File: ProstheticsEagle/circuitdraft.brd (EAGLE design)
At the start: 63 x 37 mm, 49 parts, among them IC1 BQ25887RGER, IC2 TPS54627DDAR, Q1 16 MHz

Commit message: ffff
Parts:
- L2: device rcl:0204/7 -> SamacSys_Parts:INDC2016X100N
- moved R9 2.48 mm to (41.7, 3.70)
- moved C18 1.00 mm to (42.2, 8.78)
- renumbered SERVO1 to S1, SERVO2 to S2, SERVO3 to S3, SERVO4 to S4, SERVO5 to S5

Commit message: fff
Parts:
- moved C18 0.40 mm to (41.9, 8.91)
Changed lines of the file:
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@@
 <attribute name="SPICEPREFIX" value="C" x="21.51" y="19.95" size="1.778" layer="27" rot="R90" display="off"/>
 </element>
-<element name="C18" library="rcl" library_urn="urn:adsk.eagle:library:334" package="C0805" package3d_urn="urn:adsk.eagle:package:23617/2" value="10 uF" x="42.25" y="8.78" smashed="yes">
-<attribute name="POPULARITY" value="63" x="90.51" y="-22.97" size="1.778" layer="27" display="off"/>
-<attribute name="SPICEPREFIX" value="C" x="42.25" y="8.78" size="1.778" layer="27" display="off"/>
+<element name="C18" library="rcl" library_urn="urn:adsk.eagle:library:334" package="C0805" package3d_urn="urn:adsk.eagle:package:23617/2" value="10 uF" x="41.869" y="8.907" smashed="yes">
+<attribute name="POPULARITY" value="63" x="90.129" y="-22.843" size="1.778" layer="27" display="off"/>
+<attribute name="SPICEPREFIX" value="C" x="41.869" y="8.907" size="1.778" layer="27" display="off"/>
 </element>
 <element name="C2" library="rcl" library_urn="urn:adsk.eagle:library:334" package="C0805" package3d_urn="urn:adsk.eagle:package:23617/2" value="22pF" x="25.5" y="6.66" smashed="yes" rot="R180">
@@
 </element>
 <element name="S3" library="pinhead" library_urn="urn:adsk.eagle:library:325" package="1X03" package3d_urn="urn:adsk.eagle:package:22458/2" value="" x="44.27" y="12.13" smashed="yes">
-<attribute name="NAME" x="40.6838" y="8.3788" size="1.27" layer="25" font="vector" ratio="10"/>
+<attribute name="NAME" x="49.1928" y="11.8078" size="1.27" layer="25" font="vector" ratio="10"/>
 <attribute name="POPULARITY" value="92" x="70.94" y="-39.94" size="1.778" layer="27" display="off"/>
 <attribute name="VALUE" x="40.46" y="8.955" size="1.27" layer="27"/>
@@
 <contactref element="L2" pad="1"/>
 <contactref element="C18" pad="1"/>
-<wire x1="37.08" y1="6.78" x2="41.3" y2="8.78" width="0" layer="19" extent="1-1"/>
+<wire x1="37.08" y1="6.78" x2="40.919" y2="8.907" width="0" layer="19" extent="1-1"/>
 <wire x1="35.14" y1="11.56" x2="37.08" y2="6.78" width="0" layer="19" extent="1-1"/>
 </signal>

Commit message: aa
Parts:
- C11, C12: value 22 pF -> 22 uF
- C4, C5: value 10 pF -> 10 uF
- C6: value .1 pF -> .1 uF
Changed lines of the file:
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@@
 <attribute name="SPICEPREFIX" value="C" x="70.33" y="19.02" size="1.778" layer="27" rot="R90" display="off"/>
 </element>
-<element name="C11" library="rcl" library_urn="urn:adsk.eagle:library:334" package="C0805" package3d_urn="urn:adsk.eagle:package:23617/2" value="22 pF" x="46.49" y="7.48" smashed="yes">
+<element name="C11" library="rcl" library_urn="urn:adsk.eagle:library:334" package="C0805" package3d_urn="urn:adsk.eagle:package:23617/2" value="22 uF" x="46.49" y="7.48" smashed="yes">
 <attribute name="NAME" x="48.539" y="7.258" size="1.27" layer="25" font="vector" ratio="10"/>
 <attribute name="POPULARITY" value="63" x="69.35" y="-24.27" size="1.778" layer="27" display="off"/>
 <attribute name="SPICEPREFIX" value="C" x="46.49" y="7.48" size="1.778" layer="27" display="off"/>
 </element>
-<element name="C12" library="rcl" library_urn="urn:adsk.eagle:library:334" package="C0805" package3d_urn="urn:adsk.eagle:package:23617/2" value="22 pF" x="46.86" y="4.97" smashed="yes">
+<element name="C12" library="rcl" library_urn="urn:adsk.eagle:library:334" package="C0805" package3d_urn="urn:adsk.eagle:package:23617/2" value="22 uF" x="46.86" y="4.97" smashed="yes">
 <attribute name="NAME" x="49.009" y="4.348" size="1.27" layer="25" font="vector" ratio="10"/>
 <attribute name="POPULARITY" value="63" x="76.07" y="-26.78" size="1.778" layer="27" display="off"/>
@@
 <attribute name="SPICEPREFIX" value="C" x="18" y="6.29" size="1.778" layer="27" display="off"/>
 </element>
-<element name="C4" library="rcl" library_urn="urn:adsk.eagle:library:334" package="C0805" package3d_urn="urn:adsk.eagle:package:23617/2" value="10 pF" x="67.98" y="27.23" smashed="yes" rot="R180">
+<element name="C4" library="rcl" library_urn="urn:adsk.eagle:library:334" package="C0805" package3d_urn="urn:adsk.eagle:package:23617/2" value="10 uF" x="67.98" y="27.23" smashed="yes" rot="R180">
 <attribute name="NAME" x="65.731" y="27.752" size="1.27" layer="25" font="vector" ratio="10" rot="R180"/>
 <attribute name="POPULARITY" value="63" x="12.1" y="51.36" size="1.778" layer="27" rot="R180" display="off"/>
 <attribute name="SPICEPREFIX" value="C" x="67.98" y="27.23" size="1.778" layer="27" rot="R180" display="off"/>
 </element>
-<element name="C5" library="rcl" library_urn="urn:adsk.eagle:library:334" package="C0805" package3d_urn="urn:adsk.eagle:package:23617/2" value="10 pF" x="29.84" y="7.54" smashed="yes">
+<element name="C5" library="rcl" library_urn="urn:adsk.eagle:library:334" package="C0805" package3d_urn="urn:adsk.eagle:package:23617/2" value="10 uF" x="29.84" y="7.54" smashed="yes">
 <attribute name="NAME" x="32.169" y="6.678" size="1.27" layer="25" font="vector" ratio="10"/>
 <attribute name="POPULARITY" value="63" x="92.07" y="-16.59" size="1.778" layer="27" display="off"/>
 <attribute name="SPICEPREFIX" value="C" x="29.84" y="7.54" size="1.778" layer="27" display="off"/>
 </element>
-<element name="C6" library="rcl" library_urn="urn:adsk.eagle:library:334" package="C0805" package3d_urn="urn:adsk.eagle:package:23617/2" value=".1 pF" x="28.39" y="3.09" smashed="yes" rot="R90">
+<element name="C6" library="rcl" library_urn="urn:adsk.eagle:library:334" package="C0805" package3d_urn="urn:adsk.eagle:package:23617/2" value=".1 uF" x="28.39" y="3.09" smashed="yes" rot="R90">
 <attribute name="NAME" x="28.912" y="5.139" size="1.27" layer="25" font="vector" ratio="10" rot="R90"/>
 <attribute name="POPULARITY" value="63" x="60.14" y="57.7" size="1.778" layer="27" rot="R90" display="off"/>

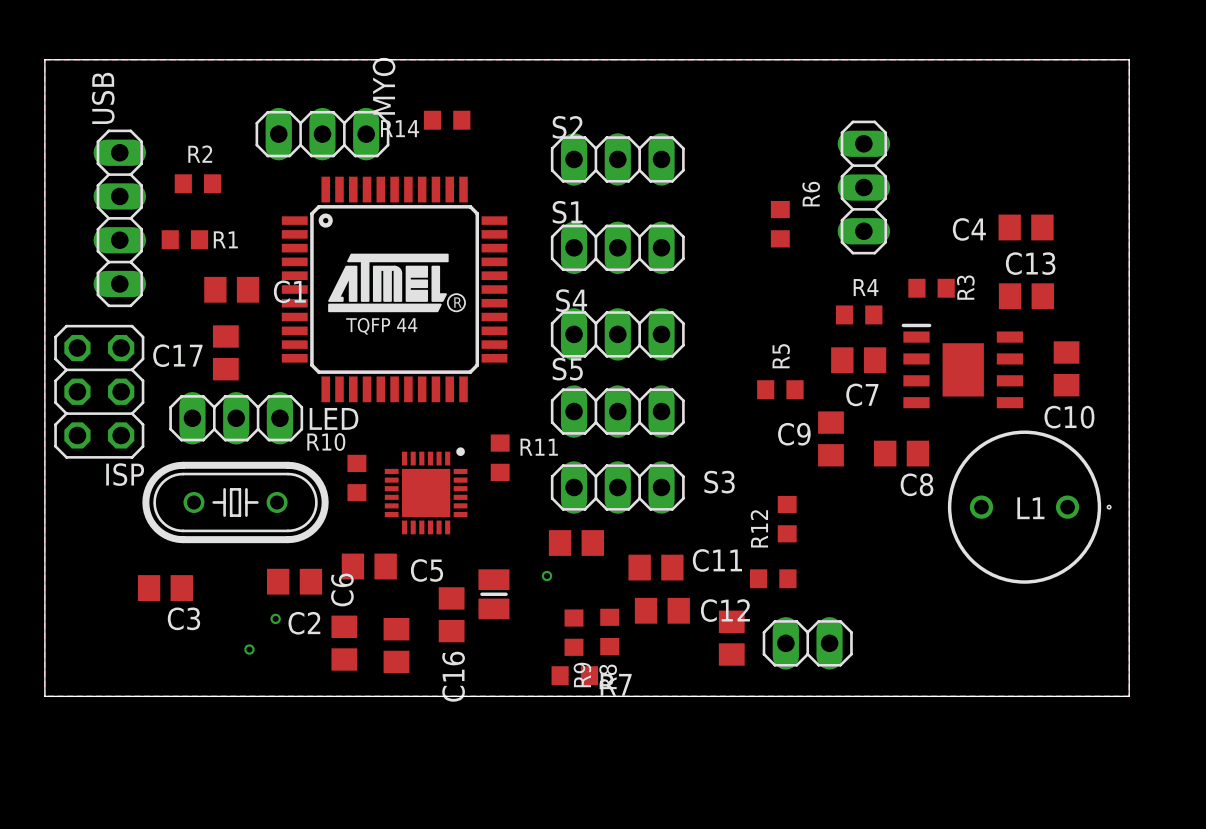
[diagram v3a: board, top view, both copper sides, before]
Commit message: added new inductor
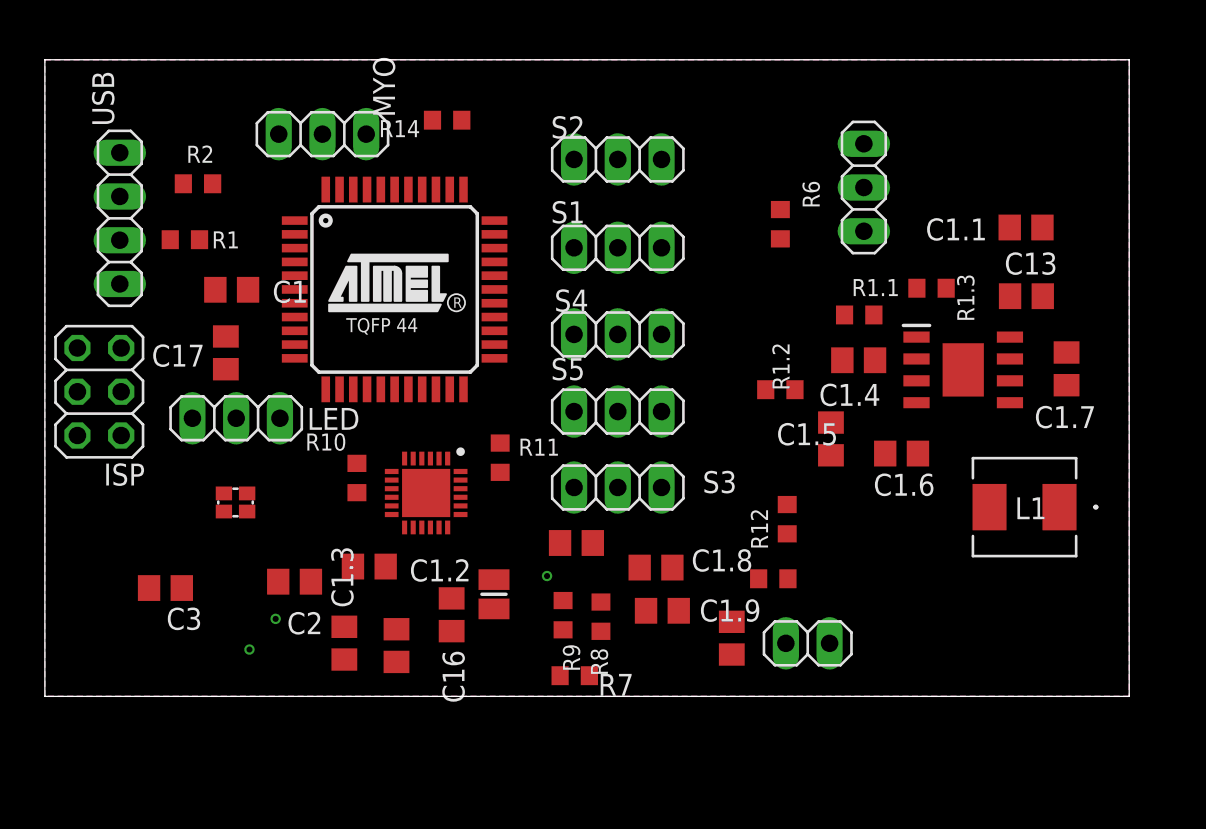
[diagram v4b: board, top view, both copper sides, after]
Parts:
- L1: value RLB0912-3R3ML -> IHLP2020CZER3R3M01; device SamacSys_Parts:RLB0914 -> ind2:IND_IHLP-2020CZ
- Q1: device crystal:HC49/S -> crystal-geyer_V1_0:2.0X1.6_KX-5
- moved R9 1.20 mm to (41.1, 4.71)
- moved R8 1.02 mm to (43.3, 4.63)
- renumbered C10 to C1.7, C11 to C1.8, C12 to C1.9, C4 to C1.1, C5 to C1.2, C6 to C1.3, C7 to C1.4, C8 to C1.6, C9 to C1.5, R3 to R1.3, R4 to R1.1, R5 to R1.2
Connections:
- net N$14: now also L1.2; no longer L1.1
- net N$6: now also Q1.3; no longer Q1.2
- net POWER: now also L1.1; no longer L1.2

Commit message: Put things closer to closer
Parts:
- moved R6 33.9 mm to (25.5, 8.50), turned to 0 degrees
- moved C1.3 33.9 mm to (60.5, 13.9)
- moved C1.2 33.6 mm to (62.8, 14.0), turned to 90 degrees
- moved C14 25.2 mm to (25.9, 6.26), turned to 180 degrees
- moved BATIO 23.2 mm to (67.6, 8.21)
- moved C13 20.2 mm to (57.2, 6.22)
- moved S3 20.1 mm to (43.8, 32.2)
- moved L1 16.3 mm to (53.9, 19.4), turned to 0 degrees
- moved R1.2 15.8 mm to (69.5, 17.6), turned to 0 degrees
- moved R8 15.3 mm to (31.0, 13.6)
- moved R7 15.2 mm to (33.1, 13.7), turned to 90 degrees
- moved C1.1 13.7 mm to (65.1, 13.8), turned to 90 degrees
- moved C1.5 13.5 mm to (69.3, 19.7), turned to 0 degrees
- moved C1.7 11.9 mm to (58.4, 19.3), turned to 270 degrees
- moved LED 11.5 mm to (14.1, 7.89), turned to 90 degrees
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
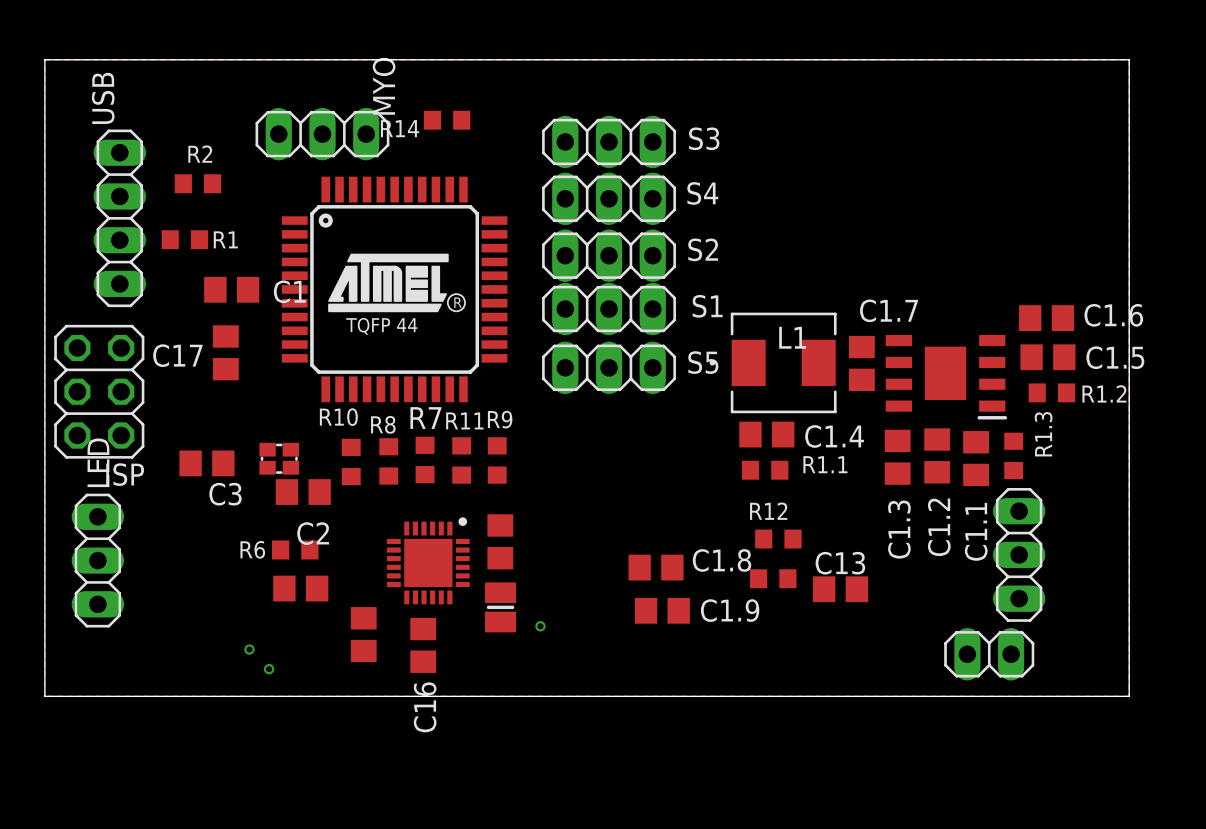
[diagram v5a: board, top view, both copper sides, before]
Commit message: Reorganized alot of things. Created different grounds
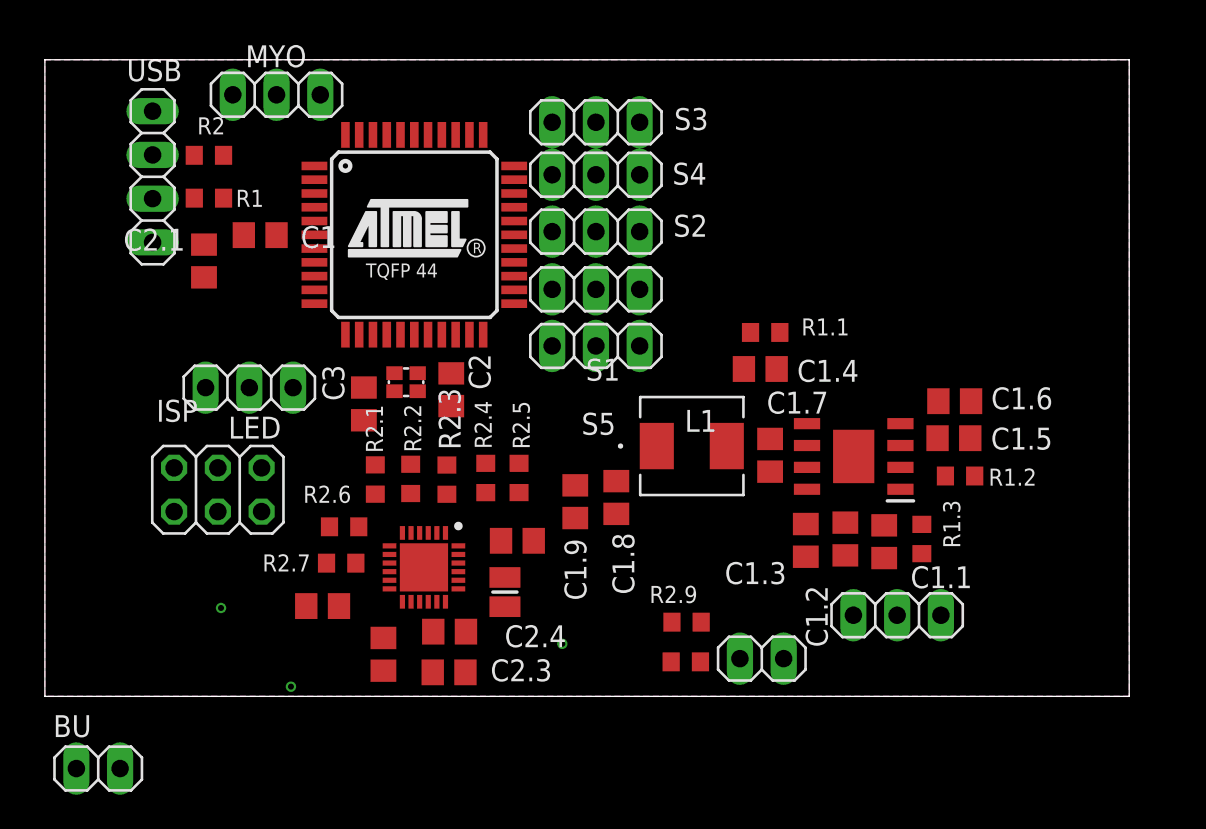
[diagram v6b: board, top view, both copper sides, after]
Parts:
- removed C13, C17: 1 uF, rcl:C0805
- removed C14: 4.7 uF, rcl:C0805
- removed C15: 47 nF, rcl:C0805
- removed C16: 44 uF, rcl:C0805
- removed C18: 10 uF, rcl:C0805
- removed R10, R11, R7, R8, R9: 10000 Ohms, rcl:R0603
- removed R12: 30.1 kOhms, rcl:R0603
- removed R13: 5.23 kOhms, rcl:R0603
- removed R14: 300 Ohms, rcl:R0603
- removed R6: 12 Ohms, rcl:R0603
- added BU: (no value), pinhead:1X02
- added C2.1, C2.3: 1 uF, rcl:C0805
- added C2.2: 4.7 uF, rcl:C0805
- added C2.4: 44 uF, rcl:C0805
- added C2.5: 47 nF, rcl:C0805
- added C2.6: 10 uF, rcl:C0805
- added R2.1, R2.2, R2.3, R2.4, R2.5: 10000 Ohms, rcl:R0603
- added R2.6: 300 Ohms, rcl:R0603
- added R2.7: 12 Ohms, rcl:R0603
- added R2.8: 5.23 kOhms, rcl:R0603
- added R2.9: 30.1 kOhms, rcl:R0603
- moved LED 13.3 mm to (22.9, 17.9), turned to 0 degrees
- moved TS 13.2 mm to (52.6, 2.19)
- moved C2 10.4 mm to (34.6, 17.8), turned to 90 degrees
- moved C3 9.74 mm to (29.5, 17.0), turned to 90 degrees
- moved ISP 8.93 mm to (21.0, 12.0), turned to 0 degrees
- moved Q1 8.60 mm to (32.0, 18.2)
- moved C1.9 8.11 mm to (41.8, 11.3), turned to 270 degrees
- moved R1.1 8.00 mm to (52.8, 21.1)
- moved BATIO 7.90 mm to (60.5, 4.71), turned to 180 degrees
- moved C1.7 7.54 mm to (53.1, 14.0)
- moved C1.5 7.20 mm to (63.8, 15.0)
- moved C1.3 7.19 mm to (55.2, 9.06)
- moved C1.6 7.19 mm to (63.8, 17.1)
- moved IC2 7.19 mm to (58.0, 13.9)
- moved R1.2 7.19 mm to (64.1, 12.8)
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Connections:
- new net GND: BATIO.3, C1.1.1, C1.2, C1.2.1, C1.3.1, C1.5.2, C1.8.2, C1.9.2, C2.1, C2.1.1, C2.2.2, C2.3.1, C2.4.2, C2.6.2, C3.1, IC1.20, IC1.8, IC2.5, IC2.9, ISP.6, LED.2, MYO.2, R2.9.1, S1.3, S2.3, S3.3, S4.3, S5.3, TS.2, U$1.23
- new net INTERRUPT?: U$1.20
- net AGND: no longer BATIO.3, C1.1.1, C1.2, C1.2.1, C1.3.1, C1.5.2, C1.8.2, C1.9.2, C13.1, C14.2, C16.2, C17.1, C18.2, C2.1, C3.1, IC1.20, IC1.8, IC2.5, IC2.9, ISP.6, LED.2, MYO.2, R12.1, S1.3, S2.3, S3.3, S4.3, S5.3, TS.2, U$1.23
- net B+: now also C2.3.2; no longer C13.2
- net BTST: now also C2.5.2; no longer C15.2
- net INT: now also R2.1.1; no longer R10.1
- net MIDDLE: now also R2.6.1, R2.7.1; no longer R14.1, R6.1
- net N$10: now also R2.6.2; no longer R14.2
- net N$18: now also C2.5.1; no longer C15.1
- net N$19: now also C2.2.1, R2.8.2; no longer C14.1, R13.2
- net N$20: now also C2.4.1; no longer C16.1
- net N$21: now also C2.6.1; no longer C18.1
- net N$3: now also R2.7.2; no longer R6.2
- net N$7: now also R2.5.1; no longer R9.1
- net SCL: now also R2.2.1; no longer R8.1
- net SDA: now also R2.3.1; no longer R7.1
- net STAT: now also R2.4.1; no longer R11.1
- net TS: now also R2.8.1, R2.9.2; no longer R12.2, R13.1
- net VBUS: now also C2.1.2, R2.1.2, R2.2.2, R2.3.2, R2.4.2, R2.5.2; no longer C17.2, R10.2, R11.2, R7.2, R8.2, R9.2
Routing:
- added copper zone on layer 1, net GND
- added copper zone on layer 16, net GND
- removed copper zone on layer 1, net AGND
- removed copper zone on layer 16, net AGND

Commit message: Ahmad's changes
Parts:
- C1.5, C1.6: device rcl:C0805 -> rcl:C0603
- moved R2.5 15.2 mm to (23.9, 16.8), turned to 180 degrees
- moved R2.4 12.9 mm to (23.9, 14.9), turned to 180 degrees
- moved R2.3 10.4 mm to (24.0, 12.6), turned to 180 degrees
- moved ISP 10.4 mm to (15.3, 20.6)
- moved R2.2 8.56 mm to (23.9, 10.5), turned to 180 degrees
- moved R2.1 7.45 mm to (24.0, 8.47), turned to 180 degrees
- moved IC1 4.60 mm to (33.5, 12.1)
- moved C1.6 2.26 mm to (65.9, 18.0)
- moved LED 2.03 mm to (22.9, 20.0)
- moved R1.2 1.74 mm to (65.9, 12.5)
- moved C1 1.39 mm to (23.6, 25.4), turned to 270 degrees
- moved C1.5 0.76 mm to (64.6, 15.0)
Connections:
- removed net AGND: C1.6.2, R1.2.2
- net GND: now also C1.6.2, R1.2.2
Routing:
- net N$11: track 0.00 -> 18.8 mm, vias 0 -> 2
- net GND: track 0.00 -> 12.8 mm
- net SDA: track 0.00 -> 11.0 mm, vias 0 -> 2
- net N$9: track 0.00 -> 5.74 mm
- net N$13: track 0.00 -> 3.20 mm
